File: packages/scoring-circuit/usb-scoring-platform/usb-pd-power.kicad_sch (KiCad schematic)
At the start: 34 parts, among them J12 PD service: GND SDA SCL, Q4 BSS138, Q5 BSS138, U19 LMR36510ADDAR, U20 TPS259470LRPWR, U5 STUSB4500QTR, U6 REC30K-2405SZ

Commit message: feat(scoring-circuit): complete nominal capacitor selections
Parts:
- C43, C44: MPN (none) -> GRM32ER71E226KE15L; Manufacturer (none) -> Murata
- C47: MPN (none) -> C3225X7R1H106K250AC; Manufacturer (none) -> TDK
- C49: MPN (none) -> C3216X7R1C106K160AC; Manufacturer (none) -> TDK
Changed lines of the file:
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@@
 (wire (pts (xy 415.29 153.67) (xy 415.29 158.75)) (stroke (width 0) (type default)))
 (global_label "USB_GND" (shape bidirectional) (at 415.29 158.75 0) (effects (font (size .9 .9)) (justify left)) (property "Intersheetrefs" "" (at 415.29 158.75 0) (effects (font (size 1 1)) (hide yes))))
-(symbol (lib_id "Device:C") (at 415.29 149.86 0) (unit 1) (in_bom yes) (on_board yes) (dnp no) (property "Reference" "C43" (at 415.29 133.35000000000002 0) (effects (font (size 1.2 1.2)))) (property "Value" "22uF 25V X7R" (at 415.29 135.89000000000001 0) (effects (font (size 1.1 1.1)))) (property "Footprint" "Capacitor_SMD:C_1210_3225Metric" (at 415.29 149.86 0) (effects (font (size 1 1)) (hide yes))) (property "Datasheet" "" (at 415.29 149.86 0) (effects (font (size 1 1)) (hide yes))) (instances (project "usb-scoring-platform" (path "/20cc8167-128c-446a-a106-f942323e143f/972b77fe-bd38-49a7-88fc-3c741d64cdb1" (reference "C43") (unit 1)))) (pin "1") (pin "2"))
+(symbol (lib_id "Device:C") (at 415.29 149.86 0) (unit 1) (in_bom yes) (on_board yes) (dnp no) (property "Reference" "C43" (at 415.29 133.35000000000002 0) (effects (font (size 1.2 1.2)))) (property "Value" "22uF 25V X7R" (at 415.29 135.89000000000001 0) (effects (font (size 1.1 1.1)))) (property "Footprint" "Capacitor_SMD:C_1210_3225Metric" (at 415.29 149.86 0) (effects (font (size 1 1)) (hide yes))) (property "Datasheet" "https://www.murata.com/en-global/api/pdfdownloadapi?cate=luCeramicCapacitorsSMD&partno=GRM32ER71E226KE15%23" (at 415.29 149.86 0) (effects (font (size 1 1)) (hide yes))) (property "Manufacturer" "Murata" (at 0 0 0) (effects (font (size 1 1)) (hide yes))) (property "MPN" "GRM32ER71E226KE15L" (at 0 0 0) (effects (font (size 1 1)) (hide yes))) (instances (project "usb-scoring-platform" (path "/20cc8167-128c-446a-a106-f942323e143f/972b77fe-bd38-49a7-88fc-3c741d64cdb1" (reference "C43") (unit 1)))) (pin "1") (pin "2"))
 (wire (pts (xy 464.82 146.05) (xy 464.82 140.97)) (stroke (width 0) (type default)))
 (global_label "USB_PRIMARY_5V" (shape bidirectional) (at 464.82 140.97 0) (effects (font (size .9 .9)) (justify left)) (property "Intersheetrefs" "" (at 464.82 140.97 0) (effects (font (size 1 1)) (hide yes))))
 (wire (pts (xy 464.82 153.67) (xy 464.82 158.75)) (stroke (width 0) (type default)))
 (global_label "USB_GND" (shape bidirectional) (at 464.82 158.75 0) (effects (font (size .9 .9)) (justify left)) (property "Intersheetrefs" "" (at 464.82 158.75 0) (effects (font (size 1 1)) (hide yes))))
-(symbol (lib_id "Device:C") (at 464.82 149.86 0) (unit 1) (in_bom yes) (on_board yes) (dnp no) (property "Reference" "C44" (at 464.82 133.35000000000002 0) (effects (font (size 1.2 1.2)))) (property "Value" "22uF 25V X7R" (at 464.82 135.89000000000001 0) (effects (font (size 1.1 1.1)))) (property "Footprint" "Capacitor_SMD:C_1210_3225Metric" (at 464.82 149.86 0) (effects (font (size 1 1)) (hide yes))) (property "Datasheet" "" (at 464.82 149.86 0) (effects (font (size 1 1)) (hide yes))) (instances (project "usb-scoring-platform" (path "/20cc8167-128c-446a-a106-f942323e143f/972b77fe-bd38-49a7-88fc-3c741d64cdb1" (reference "C44") (unit 1)))) (pin "1") (pin "2"))
+(symbol (lib_id "Device:C") (at 464.82 149.86 0) (unit 1) (in_bom yes) (on_board yes) (dnp no) (property "Reference" "C44" (at 464.82 133.35000000000002 0) (effects (font (size 1.2 1.2)))) (property "Value" "22uF 25V X7R" (at 464.82 135.89000000000001 0) (effects (font (size 1.1 1.1)))) (property "Footprint" "Capacitor_SMD:C_1210_3225Metric" (at 464.82 149.86 0) (effects (font (size 1 1)) (hide yes))) (property "Datasheet" "https://www.murata.com/en-global/api/pdfdownloadapi?cate=luCeramicCapacitorsSMD&partno=GRM32ER71E226KE15%23" (at 464.82 149.86 0) (effects (font (size 1 1)) (hide yes))) (property "Manufacturer" "Murata" (at 0 0 0) (effects (font (size 1 1)) (hide yes))) (property "MPN" "GRM32ER71E226KE15L" (at 0 0 0) (effects (font (size 1 1)) (hide yes))) (instances (project "usb-scoring-platform" (path "/20cc8167-128c-446a-a106-f942323e143f/972b77fe-bd38-49a7-88fc-3c741d64cdb1" (reference "C44") (unit 1)))) (pin "1") (pin "2"))
 (wire (pts (xy 415.29 81.28) (xy 415.29 76.2)) (stroke (width 0) (type default)))
 (global_label "USB_PRIMARY_5V" (shape bidirectional) (at 415.29 76.2 0) (effects (font (size .9 .9)) (justify left)) (property "Intersheetrefs" "" (at 415.29 76.2 0) (effects (font (size 1 1)) (hide yes))))
@@
 (wire (pts (xy 519.43 313.69) (xy 519.43 318.77)) (stroke (width 0) (type default)))
 (global_label "USB_GND" (shape bidirectional) (at 519.43 318.77 0) (effects (font (size .9 .9)) (justify left)) (property "Intersheetrefs" "" (at 519.43 318.77 0) (effects (font (size 1 1)) (hide yes))))
-(symbol (lib_id "Device:C") (at 519.43 309.88 0) (unit 1) (in_bom yes) (on_board yes) (dnp no) (property "Reference" "C47" (at 519.43 293.37 0) (effects (font (size 1.2 1.2)))) (property "Value" "10uF 50V" (at 519.43 295.90999999999997 0) (effects (font (size 1.1 1.1)))) (property "Footprint" "Capacitor_SMD:C_1210_3225Metric" (at 519.43 309.88 0) (effects (font (size 1 1)) (hide yes))) (property "Datasheet" "" (at 519.43 309.88 0) (effects (font (size 1 1)) (hide yes))) (instances (project "usb-scoring-platform" (path "/20cc8167-128c-446a-a106-f942323e143f/972b77fe-bd38-49a7-88fc-3c741d64cdb1" (reference "C47") (unit 1)))) (pin "1") (pin "2"))
+(symbol (lib_id "Device:C") (at 519.43 309.88 0) (unit 1) (in_bom yes) (on_board yes) (dnp no) (property "Reference" "C47" (at 519.43 293.37 0) (effects (font (size 1.2 1.2)))) (property "Value" "10uF 50V" (at 519.43 295.90999999999997 0) (effects (font (size 1.1 1.1)))) (property "Footprint" "Capacitor_SMD:C_1210_3225Metric" (at 519.43 309.88 0) (effects (font (size 1 1)) (hide yes))) (property "Datasheet" "https://product.tdk.com/en/search/capacitor/ceramic/mlcc/info?part_no=C3225X7R1H106K250AC" (at 519.43 309.88 0) (effects (font (size 1 1)) (hide yes))) (property "Manufacturer" "TDK" (at 0 0 0) (effects (font (size 1 1)) (hide yes))) (property "MPN" "C3225X7R1H106K250AC" (at 0 0 0) (effects (font (size 1 1)) (hide yes))) (instances (project "usb-scoring-platform" (path "/20cc8167-128c-446a-a106-f942323e143f/972b77fe-bd38-49a7-88fc-3c741d64cdb1" (reference "C47") (unit 1)))) (pin "1") (pin "2"))
 (wire (pts (xy 464.82 360.68) (xy 464.82 355.6)) (stroke (width 0) (type default)))
 (global_label "PANEL_5V" (shape bidirectional) (at 464.82 355.6 0) (effects (font (size .9 .9)) (justify left)) (property "Intersheetrefs" "" (at 464.82 355.6 0) (effects (font (size 1 1)) (hide yes))))
@@
 (wire (pts (xy 519.43 368.3) (xy 519.43 373.38)) (stroke (width 0) (type default)))
 (global_label "GND" (shape bidirectional) (at 519.43 373.38 0) (effects (font (size .9 .9)) (justify left)) (property "Intersheetrefs" "" (at 519.43 373.38 0) (effects (font (size 1 1)) (hide yes))))
-(symbol (lib_id "Device:C") (at 519.43 364.49 0) (unit 1) (in_bom yes) (on_board yes) (dnp no) (property "Reference" "C49" (at 519.43 347.98 0) (effects (font (size 1.2 1.2)))) (property "Value" "10uF 16V X7R" (at 519.43 350.52 0) (effects (font (size 1.1 1.1)))) (property "Footprint" "Capacitor_SMD:C_1206_3216Metric" (at 519.43 364.49 0) (effects (font (size 1 1)) (hide yes))) (property "Datasheet" "" (at 519.43 364.49 0) (effects (font (size 1 1)) (hide yes))) (instances (project "usb-scoring-platform" (path "/20cc8167-128c-446a-a106-f942323e143f/972b77fe-bd38-49a7-88fc-3c741d64cdb1" (reference "C49") (unit 1)))) (pin "1") (pin "2"))
+(symbol (lib_id "Device:C") (at 519.43 364.49 0) (unit 1) (in_bom yes) (on_board yes) (dnp no) (property "Reference" "C49" (at 519.43 347.98 0) (effects (font (size 1.2 1.2)))) (property "Value" "10uF 16V X7R" (at 519.43 350.52 0) (effects (font (size 1.1 1.1)))) (property "Footprint" "Capacitor_SMD:C_1206_3216Metric" (at 519.43 364.49 0) (effects (font (size 1 1)) (hide yes))) (property "Datasheet" "https://product.tdk.com/en/search/capacitor/ceramic/mlcc/info?part_no=C3216X7R1C106K160AC" (at 519.43 364.49 0) (effects (font (size 1 1)) (hide yes))) (property "Manufacturer" "TDK" (at 0 0 0) (effects (font (size 1 1)) (hide yes))) (property "MPN" "C3216X7R1C106K160AC" (at 0 0 0) (effects (font (size 1 1)) (hide yes))) (instances (project "usb-scoring-platform" (path "/20cc8167-128c-446a-a106-f942323e143f/972b77fe-bd38-49a7-88fc-3c741d64cdb1" (reference "C49") (unit 1)))) (pin "1") (pin "2"))
 (wire (pts (xy 184.15 365.76) (xy 184.15 360.68)) (stroke (width 0) (type default)))
 (global_label "USB_VBUS" (shape bidirectional) (at 184.15 360.68 0) (effects (font (size .9 .9)) (justify left)) (property "Intersheetrefs" "" (at 184.15 360.68 0) (effects (font (size 1 1)) (hide yes))))

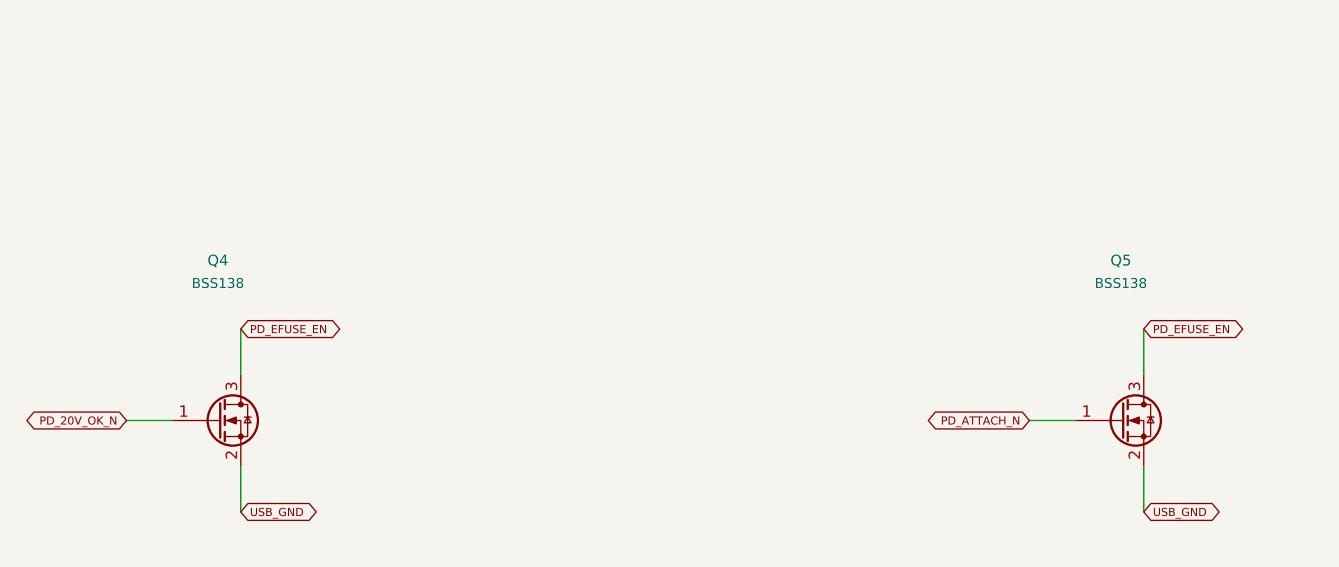
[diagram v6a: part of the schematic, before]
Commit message: fix(scoring-circuit): select low-voltage switching transistors
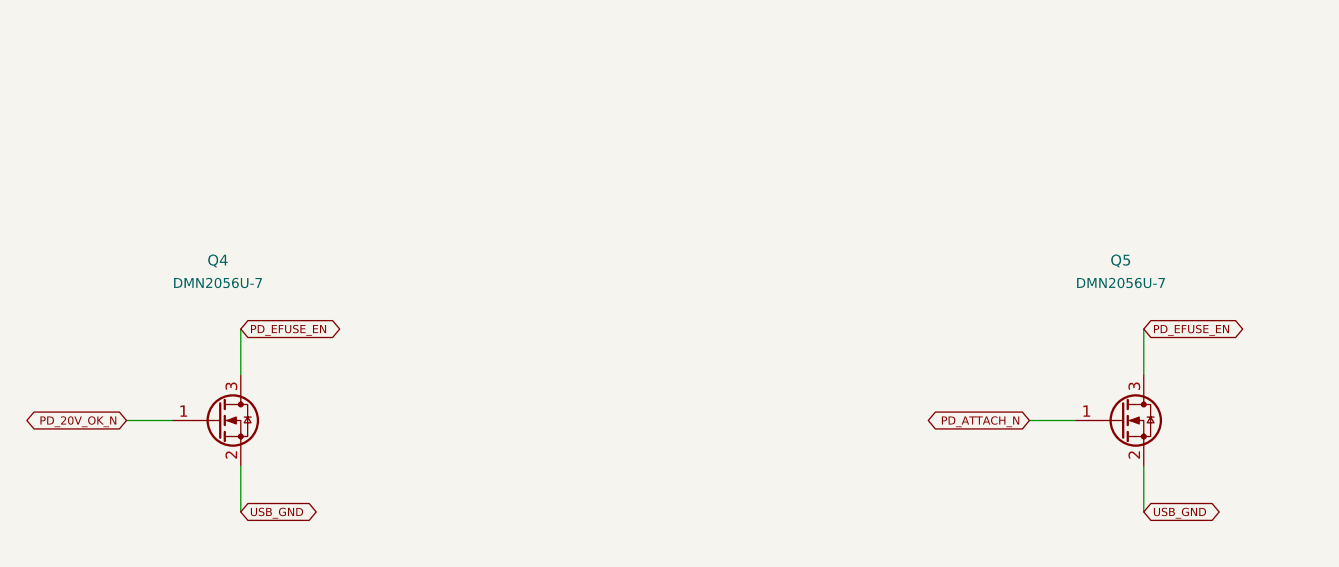
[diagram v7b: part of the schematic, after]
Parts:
- Q4, Q5: value BSS138 -> DMN2056U-7; MPN (none) -> DMN2056U-7; Manufacturer (none) -> Diodes Incorporated
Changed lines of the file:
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@@
 (wire (pts (xy 67.31 240.03) (xy 67.31 234.95)) (stroke (width 0) (type default)))
 (global_label "PD_EFUSE_EN" (shape bidirectional) (at 67.31 234.95 0) (effects (font (size .9 .9)) (justify left)) (property "Intersheetrefs" "" (at 67.31 234.95 0) (effects (font (size 1 1)) (hide yes))))
-(symbol (lib_id "Transistor_FET:BSS138") (at 64.77 245.11 0) (unit 1) (in_bom yes) (on_board yes) (dnp no) (property "Reference" "Q4" (at 64.77 227.33 0) (effects (font (size 1.2 1.2)))) (property "Value" "BSS138" (at 64.77 229.87 0) (effects (font (size 1.1 1.1)))) (property "Footprint" "Package_TO_SOT_SMD:SOT-23" (at 64.77 245.11 0) (effects (font (size 1 1)) (hide yes))) (property "Datasheet" "https://www.onsemi.com/pub/Collateral/BSS138-D.PDF" (at 64.77 245.11 0) (effects (font (size 1 1)) (hide yes))) (instances (project "usb-scoring-platform" (path "/20cc8167-128c-446a-a106-f942323e143f/972b77fe-bd38-49a7-88fc-3c741d64cdb1" (reference "Q4") (unit 1)))) (pin "1") (pin "2") (pin "3"))
+(symbol (lib_id "Transistor_FET:BSS138") (at 64.77 245.11 0) (unit 1) (in_bom yes) (on_board yes) (dnp no) (property "Reference" "Q4" (at 64.77 227.33 0) (effects (font (size 1.2 1.2)))) (property "Value" "DMN2056U-7" (at 64.77 229.87 0) (effects (font (size 1.1 1.1)))) (property "Footprint" "Package_TO_SOT_SMD:SOT-23" (at 64.77 245.11 0) (effects (font (size 1 1)) (hide yes))) (property "Datasheet" "https://www.diodes.com/datasheet/download/DMN2056U.pdf" (at 64.77 245.11 0) (effects (font (size 1 1)) (hide yes))) (instances (project "usb-scoring-platform" (path "/20cc8167-128c-446a-a106-f942323e143f/972b77fe-bd38-49a7-88fc-3c741d64cdb1" (reference "Q4") (unit 1)))) (pin "1") (pin "2") (pin "3") (property "Manufacturer" "Diodes Incorporated" (at 0 0 0) (effects (font (size 1 1)) (hide yes))) (property "MPN" "DMN2056U-7" (at 0 0 0) (effects (font (size 1 1)) (hide yes))))
 (wire (pts (xy 160.02 245.11) (xy 154.94 245.11)) (stroke (width 0) (type default)))
 (global_label "PD_ATTACH_N" (shape bidirectional) (at 154.94 245.11 180) (effects (font (size .9 .9)) (justify right)) (property "Intersheetrefs" "" (at 154.94 245.11 180) (effects (font (size 1 1)) (hide yes))))
@@
 (wire (pts (xy 167.64 240.03) (xy 167.64 234.95)) (stroke (width 0) (type default)))
 (global_label "PD_EFUSE_EN" (shape bidirectional) (at 167.64 234.95 0) (effects (font (size .9 .9)) (justify left)) (property "Intersheetrefs" "" (at 167.64 234.95 0) (effects (font (size 1 1)) (hide yes))))
-(symbol (lib_id "Transistor_FET:BSS138") (at 165.1 245.11 0) (unit 1) (in_bom yes) (on_board yes) (dnp no) (property "Reference" "Q5" (at 165.1 227.33 0) (effects (font (size 1.2 1.2)))) (property "Value" "BSS138" (at 165.1 229.87 0) (effects (font (size 1.1 1.1)))) (property "Footprint" "Package_TO_SOT_SMD:SOT-23" (at 165.1 245.11 0) (effects (font (size 1 1)) (hide yes))) (property "Datasheet" "https://www.onsemi.com/pub/Collateral/BSS138-D.PDF" (at 165.1 245.11 0) (effects (font (size 1 1)) (hide yes))) (instances (project "usb-scoring-platform" (path "/20cc8167-128c-446a-a106-f942323e143f/972b77fe-bd38-49a7-88fc-3c741d64cdb1" (reference "Q5") (unit 1)))) (pin "1") (pin "2") (pin "3"))
+(symbol (lib_id "Transistor_FET:BSS138") (at 165.1 245.11 0) (unit 1) (in_bom yes) (on_board yes) (dnp no) (property "Reference" "Q5" (at 165.1 227.33 0) (effects (font (size 1.2 1.2)))) (property "Value" "DMN2056U-7" (at 165.1 229.87 0) (effects (font (size 1.1 1.1)))) (property "Footprint" "Package_TO_SOT_SMD:SOT-23" (at 165.1 245.11 0) (effects (font (size 1 1)) (hide yes))) (property "Datasheet" "https://www.diodes.com/datasheet/download/DMN2056U.pdf" (at 165.1 245.11 0) (effects (font (size 1 1)) (hide yes))) (instances (project "usb-scoring-platform" (path "/20cc8167-128c-446a-a106-f942323e143f/972b77fe-bd38-49a7-88fc-3c741d64cdb1" (reference "Q5") (unit 1)))) (pin "1") (pin "2") (pin "3") (property "Manufacturer" "Diodes Incorporated" (at 0 0 0) (effects (font (size 1 1)) (hide yes))) (property "MPN" "DMN2056U-7" (at 0 0 0) (effects (font (size 1 1)) (hide yes))))
 (wire (pts (xy 59.69 306.07) (xy 59.69 300.99)) (stroke (width 0) (type default)))
 (global_label "USB_PRIMARY_5V" (shape bidirectional) (at 59.69 300.99 0) (effects (font (size .9 .9)) (justify left)) (property "Intersheetrefs" "" (at 59.69 300.99 0) (effects (font (size 1 1)) (hide yes))))

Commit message: chore(scoring-circuit): bind reviewed power inductor ordering codes
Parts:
- L2: MPN (none) -> XAL5050-223MEC; Manufacturer (none) -> Coilcraft
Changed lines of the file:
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@@
 (wire (pts (xy 364.49 88.9) (xy 364.49 93.98)) (stroke (width 0) (type default)))
 (global_label "USB_PRIMARY_5V" (shape bidirectional) (at 364.49 93.98 0) (effects (font (size .9 .9)) (justify left)) (property "Intersheetrefs" "" (at 364.49 93.98 0) (effects (font (size 1 1)) (hide yes))))
-(symbol (lib_id "Device:L") (at 364.49 85.09 0) (unit 1) (in_bom yes) (on_board yes) (dnp no) (property "Reference" "L2" (at 364.49 68.58 0) (effects (font (size 1.2 1.2)))) (property "Value" "XAL5050-223MEC 22uH" (at 364.49 71.12 0) (effects (font (size 1.1 1.1)))) (property "Footprint" "Inductor_SMD:L_Coilcraft_XAL5050-XXX" (at 364.49 85.09 0) (effects (font (size 1 1)) (hide yes))) (property "Datasheet" "" (at 364.49 85.09 0) (effects (font (size 1 1)) (hide yes))) (instances (project "usb-scoring-platform" (path "/20cc8167-128c-446a-a106-f942323e143f/972b77fe-bd38-49a7-88fc-3c741d64cdb1" (reference "L2") (unit 1)))) (pin "1") (pin "2"))
+(symbol (lib_id "Device:L") (at 364.49 85.09 0) (unit 1) (in_bom yes) (on_board yes) (dnp no) (property "Reference" "L2" (at 364.49 68.58 0) (effects (font (size 1.2 1.2)))) (property "Value" "XAL5050-223MEC 22uH" (at 364.49 71.12 0) (effects (font (size 1.1 1.1)))) (property "Footprint" "Inductor_SMD:L_Coilcraft_XAL5050-XXX" (at 364.49 85.09 0) (effects (font (size 1 1)) (hide yes))) (property "Datasheet" "https://www.coilcraft.com/getmedia/49bc46c8-4b2c-45b9-9b6c-2eaa235ea698/xal50xx.pdf" (at 364.49 85.09 0) (effects (font (size 1 1)) (hide yes))) (instances (project "usb-scoring-platform" (path "/20cc8167-128c-446a-a106-f942323e143f/972b77fe-bd38-49a7-88fc-3c741d64cdb1" (reference "L2") (unit 1)))) (pin "1") (pin "2") (property "Manufacturer" "Coilcraft" (at 0 0 0) (effects (font (size 1 1)) (hide yes))) (property "MPN" "XAL5050-223MEC" (at 0 0 0) (effects (font (size 1 1)) (hide yes))))
 (wire (pts (xy 245.11 146.05) (xy 245.11 140.97)) (stroke (width 0) (type default)))
 (global_label "USB_VBUS" (shape bidirectional) (at 245.11 140.97 0) (effects (font (size .9 .9)) (justify left)) (property "Intersheetrefs" "" (at 245.11 140.97 0) (effects (font (size 1 1)) (hide yes))))
